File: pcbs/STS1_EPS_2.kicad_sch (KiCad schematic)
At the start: 11 parts, among them J1 DS1, J2 DS2, J5 RBF, J6 Antenna Deployment, J7 Inter-EPS, J8 UCI, U8 TPS259472ARPW

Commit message: Intermediate commit.
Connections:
- net UCI_COBC_NOT_RST: now reaches J8.10 (Pin_10)
- net UCI_COBC_SWDIO: now reaches J8.7 (Pin_7)
- net UCI_COBC_SWDCLK: now reaches J8.8 (Pin_8)
- net UCI_COBC_SWO: now reaches J8.9 (Pin_9)
- net UCI_COBC_3V3 renamed UCI_COBC_5V
- net UCI_COBC_UART_RX renamed UCI_COBC_UART_2
- net UCI_COBC_UART_TX renamed UCI_COBC_UART_1
- no-connect marks 7 -> 3
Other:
- sheet CSBI ports: added UCI_COBC_5V, UCI_COBC_NOT_RST, UCI_COBC_SWDCLK, UCI_COBC_SWDIO, UCI_COBC_SWO; removed none
- moved on the sheet: J8

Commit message: Signals to the bus gate should now be provided with supply voltage the proper way.
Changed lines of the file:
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@@
 	(wire
 		(pts
-			(xy 110.49 144.78) (xy 112.395 144.78)
+			(xy 108.585 153.67) (xy 110.49 153.67)
 		)
 		(stroke
@@
 	(wire
 		(pts
-			(xy 136.525 142.24) (xy 139.065 142.24)
+			(xy 134.62 151.13) (xy 137.16 151.13)
 		)
 		(stroke
@@
 	(wire
 		(pts
-			(xy 110.49 142.24) (xy 112.395 142.24)
+			(xy 108.585 151.13) (xy 110.49 151.13)
 		)
 		(stroke
@@
 	)
 	(label "BATT_RAW"
-		(at 110.49 144.78 180)
+		(at 108.585 153.67 180)
 		(fields_autoplaced yes)
 		(effects
@@
 	)
 	(label "MPPT_BUS"
-		(at 110.49 142.24 180)
+		(at 108.585 151.13 180)
 		(fields_autoplaced yes)
 		(effects
@@
 	)
 	(label "V_LOGIC"
-		(at 139.065 142.24 0)
+		(at 137.16 151.13 0)
 		(fields_autoplaced yes)
 		(effects
@@
 	)
 	(sheet
-		(at 112.395 140.335)
+		(at 110.49 149.225)
 		(size 24.13 6.35)
 		(fields_autoplaced yes)
@@
 		)
 		(property "Sheetname" "Logic Voltage"
-			(at 112.395 139.6234 0)
+			(at 110.49 148.5134 0)
 			(effects
 				(font
@@
 		)
 		(property "Sheetfile" "STS1_EPS_2_LOGIC_VOLTAGE.kicad_sch"
-			(at 112.395 147.2696 0)
+			(at 110.49 156.1596 0)
 			(effects
 				(font
@@
 		)
 		(pin "MPPT_BUS" input
-			(at 112.395 142.24 180)
+			(at 110.49 151.13 180)
 			(effects
 				(font
@@
 		)
 		(pin "BATT_RAW" input
-			(at 112.395 144.78 180)
+			(at 110.49 153.67 180)
 			(effects
 				(font
@@
 		)
 		(pin "V_LOGIC" output
-			(at 136.525 142.24 0)
+			(at 134.62 151.13 0)
 			(effects
 				(font

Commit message: Intermediate commit.
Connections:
- net GNDREF is gone; now on net GND: J8.2 (Pin_2)
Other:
- sheet Bus Gate ports: added V_LOGIC; removed none
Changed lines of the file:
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@@
 	(wire
 		(pts
-			(xy 44.45 180.34) (xy 43.815 180.34)
+			(xy 168.91 59.69) (xy 171.45 59.69)
 		)
 		(stroke
@@
 	(label "MPPT_BUS"
 		(at 108.585 151.13 180)
+		(fields_autoplaced yes)
+		(effects
+			(font
+				(size 1.27 1.27)
+			)
+			(justify right bottom)
+		)
+	)
+	(label "V_LOGIC"
+		(at 168.91 59.69 180)
 		(fields_autoplaced yes)
 		(effects
@@
 				(path "/38c03ff7-ea47-4d00-b37d-ddcaa7d87722"
 					(reference "#PWR03")
-					(unit 1)
-				)
-			)
-		)
-	)
-	(symbol
-		(lib_id "power:GNDREF")
-		(at 43.815 180.34 90)
-		(unit 1)
-		(exclude_from_sim no)
-		(in_bom yes)
-		(on_board yes)
-		(dnp no)
-		(fields_autoplaced yes)
-		(property "Reference" "#PWR0116"
-			(at 50.165 180.34 0)
-			(effects
-				(font
-					(size 1.27 1.27)
-				)
-				(hide yes)
-			)
-		)
-		(property "Value" "GNDREF"
-			(at 46.99 180.3399 90)
-			(effects
-				(font
-					(size 1.27 1.27)
-				)
-				(justify right)
-			)
-		)
-		(property "Footprint" ""
-			(at 43.815 180.34 0)
-			(effects
-				(font
-					(size 1.27 1.27)
-				)
-				(hide yes)
-			)
-		)
-		(property "Datasheet" ""
-			(at 43.815 180.34 0)
-			(effects
-				(font
-					(size 1.27 1.27)
-				)
-				(hide yes)
-			)
-		)
-		(property "Description" ""
-			(at 43.815 180.34 0)
-			(effects
-				(font
-					(size 1.27 1.27)
-				)
-				(hide yes)
-			)
-		)
-		(pin "1"
-		)
-		(instances
-			(project "STS1_EPS_2"
-				(path "/38c03ff7-ea47-4d00-b37d-ddcaa7d87722"
-					(reference "#PWR0116")
 					(unit 1)
 				)
@@
 				(path "/38c03ff7-ea47-4d00-b37d-ddcaa7d87722"
 					(reference "J5")
+					(unit 1)
+				)
+			)
+		)
+	)
+	(symbol
+		(lib_id "power:GND")
+		(at 44.45 180.34 90)
+		(unit 1)
+		(exclude_from_sim no)
+		(in_bom yes)
+		(on_board yes)
+		(dnp no)
+		(fields_autoplaced yes)
+		(property "Reference" "#PWR095"
+			(at 50.8 180.34 0)
+			(effects
+				(font
+					(size 1.27 1.27)
+				)
+				(hide yes)
+			)
+		)
+		(property "Value" "GND"
+			(at 47.625 180.3399 90)
+			(effects
+				(font
+					(size 1.27 1.27)
+				)
+				(justify right)
+			)
+		)
+		(property "Footprint" ""
+			(at 44.45 180.34 0)
+			(effects
+				(font
+					(size 1.27 1.27)
+				)
+				(hide yes)
+			)
+		)
+		(property "Datasheet" ""
+			(at 44.45 180.34 0)
+			(effects
+				(font
+					(size 1.27 1.27)
+				)
+				(hide yes)
+			)
+		)
+		(property "Description" ""
+			(at 44.45 180.34 0)
+			(effects
+				(font
+					(size 1.27 1.27)
+				)
+				(hide yes)
+			)
+		)
+		(pin "1"
+		)
+		(instances
+			(project "STS1_EPS_2"
+				(path "/38c03ff7-ea47-4d00-b37d-ddcaa7d87722"
+					(reference "#PWR095")
 					(unit 1)
 				)
@@
 			(effects
 				(font
+					(size 1.27 1.27)
+				)
+				(justify left)
+			)
+		)
+		(pin "V_LOGIC" input
+			(at 171.45 59.69 180)
+			(effects
+				(font

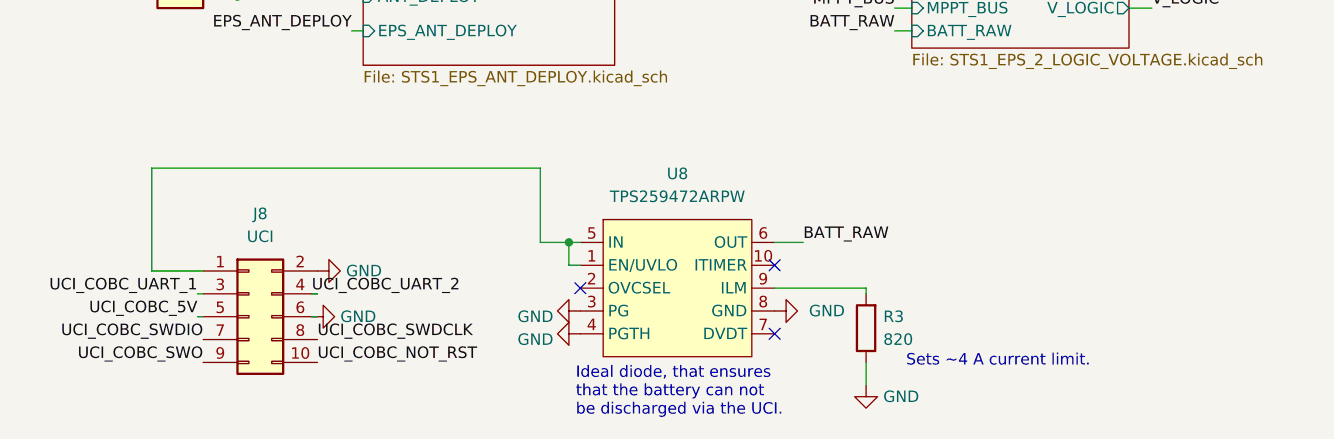
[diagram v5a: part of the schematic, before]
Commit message: Removed UCI connector from STS1_EPS_2 and merged UCI connector with J5 on STS1_EPS_1.
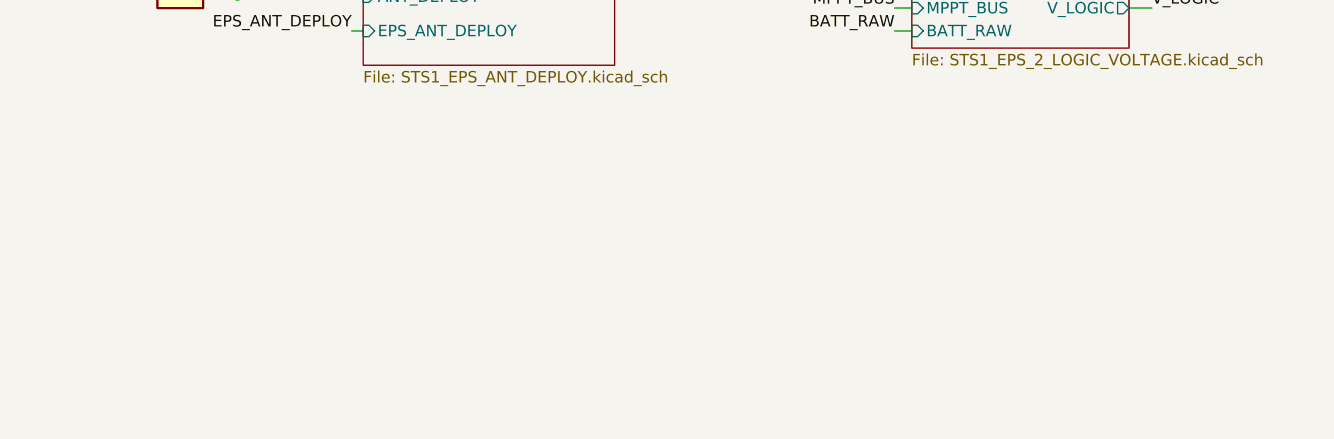
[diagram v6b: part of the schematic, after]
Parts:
- removed J8: UCI, STS_Connector:M80-85110YY, symbol Connector_Generic:Conn_02x05_Odd_Even
- removed R3: 820, Resistor_SMD:R_0805_2012Metric, symbol Device:R
- removed U8: TPS259472ARPW, STS_Package_DFN_QFN:TPS259472ARPWR, symbol STS_Power_Management:TPS259472ARPW
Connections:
- no-connect marks 3 -> 0
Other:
- note removed: "Ideal diode, that ensures that the battery can not be discharged via the UCI."
- note removed: "Sets ~4 A current limit."

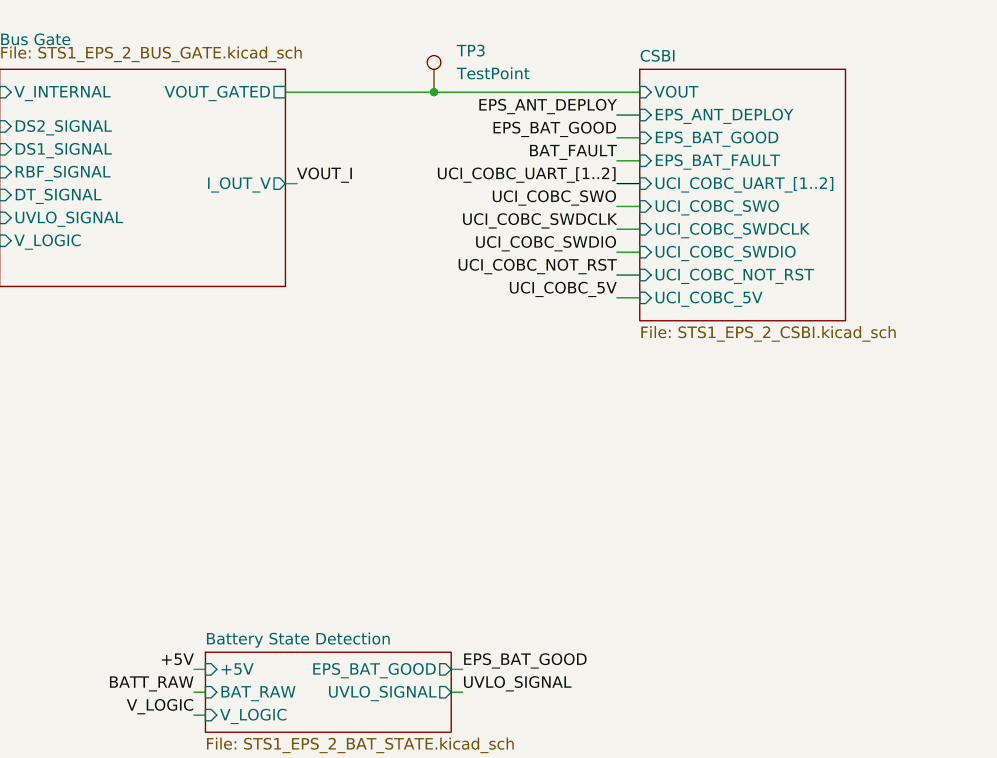
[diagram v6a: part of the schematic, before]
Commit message: Added even more ESD protection.
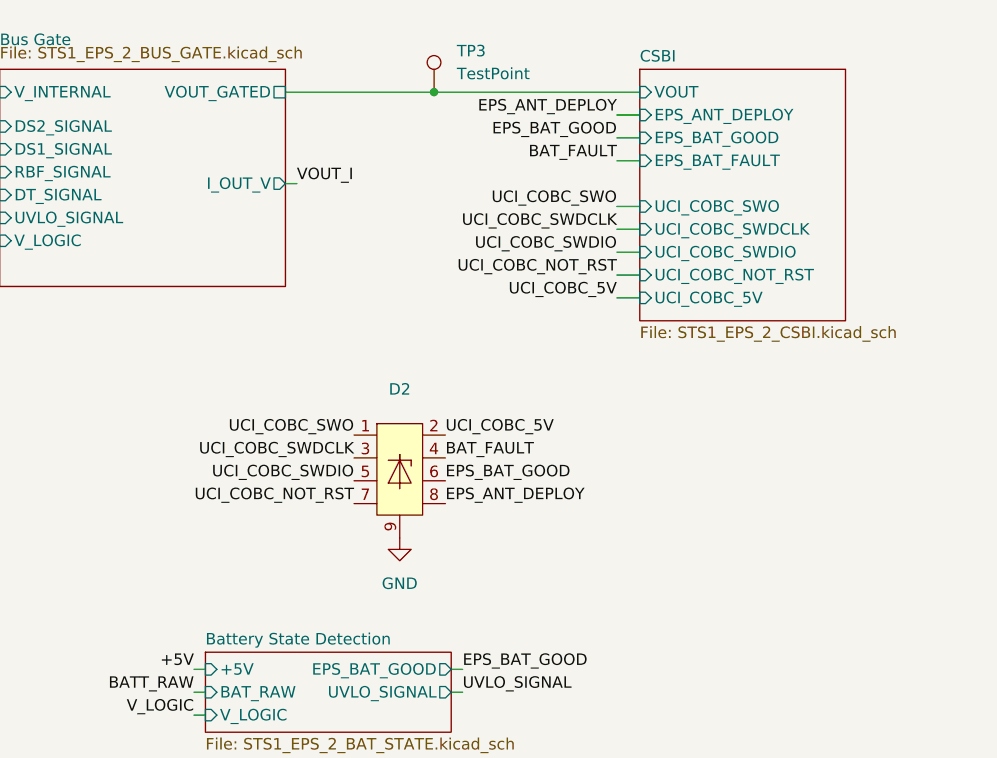
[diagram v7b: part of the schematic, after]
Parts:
- added D2: ~, STS_Misc:LLP1713-9L, symbol STS_Power_Management:VESD05A8A
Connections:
- net BAT_FAULT: now also D2.4
- net EPS_ANT_DEPLOY: now also D2.8
- net EPS_BAT_GOOD: now also D2.6
- net GND: now also D2.9
- net UCI_COBC_5V: now also D2.2
- net UCI_COBC_NOT_RST: now also D2.7
- net UCI_COBC_SWDCLK: now also D2.3
- net UCI_COBC_SWDIO: now also D2.5
- net UCI_COBC_SWO: now also D2.1
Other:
- sheet CSBI ports: added none; removed UCI_COBC_UART_[1..2]
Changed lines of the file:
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@@
-		)
-	)
-	(bus
-		(pts
-			(xy 240.03 53.34) (xy 242.57 53.34)
-		)
-		(stroke
-			(width 0)
-			(type default)
 		)
 	)
@@
 		)
 	)
+	(label "EPS_ANT_DEPLOY"
+		(at 220.98 88.9 0)
+		(fields_autoplaced yes)
+		(effects
+			(font
+				(size 1.27 1.27)
+			)
+			(justify left bottom)
+		)
+	)
+	(label "BAT_FAULT"
+		(at 220.98 83.82 0)
+		(fields_autoplaced yes)
+		(effects
+			(font
+				(size 1.27 1.27)
+			)
+			(justify left bottom)
+		)
+	)
 	(label "BAT_FAULT"
 		(at 190.5 141.605 180)
@@
 		)
 	)
-	(label "UCI_COBC_UART_[1..2]"
-		(at 240.03 53.34 180)
+	(label "UCI_COBC_SWDIO"
+		(at 210.82 86.36 180)
+		(fields_autoplaced yes)
+		(effects
+			(font
+				(size 1.27 1.27)
+			)
+			(justify right bottom)
+		)
+	)
+	(label "UCI_COBC_NOT_RST"
+		(at 210.82 88.9 180)
 		(fields_autoplaced yes)
 		(effects
@@
 		)
 	)
+	(label "UCI_COBC_5V"
+		(at 220.98 81.28 0)
+		(fields_autoplaced yes)
+		(effects
+			(font
+				(size 1.27 1.27)
+			)
+			(justify left bottom)
+		)
+	)
+	(label "EPS_BAT_GOOD"
+		(at 220.98 86.36 0)
+		(fields_autoplaced yes)
+		(effects
+			(font
+				(size 1.27 1.27)
+			)
+			(justify left bottom)
+		)
+	)
 	(label "V_LOGIC"
 		(at 109.855 92.71 180)
@@
 		)
 	)
+	(label "UCI_COBC_SWO"
+		(at 210.82 81.28 180)
+		(fields_autoplaced yes)
+		(effects
+			(font
+				(size 1.27 1.27)
+			)
+			(justify right bottom)
+		)
+	)
 	(label "EPS_BAT_GOOD"
 		(at 222.885 107.315 0)
@@
 			)
 			(justify left bottom)
+		)
+	)
+	(label "UCI_COBC_SWDCLK"
+		(at 210.82 83.82 180)
+		(fields_autoplaced yes)
+		(effects
+			(font
+				(size 1.27 1.27)
+			)
+			(justify right bottom)
 		)
 	)
@@
 	)
 	(symbol
+		(lib_id "STS_Power_Management:VESD05A8A")
+		(at 215.9 78.74 0)
+		(unit 1)
+		(exclude_from_sim no)
+		(in_bom yes)
+		(on_board yes)
+		(dnp no)
+		(fields_autoplaced yes)
+		(property "Reference" "D2"
+			(at 215.9 76.2 0)
+			(effects
+				(font
+					(size 1.27 1.27)
+				)
+			)
+		)
+		(property "Value" "~"
+			(at 215.9 78.74 0)
+			(effects
+				(font
+					(size 1.27 1.27)
+				)
+			)
+		)
+		(property "Footprint" "STS_Misc:LLP1713-9L"
+			(at 216.154 75.184 0)
+			(effects
+				(font
+					(size 1.27 1.27)
+				)
+				(hide yes)
+			)
+		)
+		(property "Datasheet" ""
+			(at 215.9 78.74 0)
+			(effects
+				(font
+					(size 1.27 1.27)
+				)
+				(hide yes)
+			)
+		)
+		(property "Description" ""
+			(at 215.9 78.74 0)
+			(effects
+				(font
+					(size 1.27 1.27)
+				)
+				(hide yes)
+			)
+		)
+		(pin "5"
+		)
+		(pin "7"
+		)
+		(pin "9"
+		)
+		(pin "8"
+		)
+		(pin "3"
+		)
+		(pin "6"
+		)
+		(pin "4"
+		)
+		(pin "1"
+		)
+		(pin "2"
+		)
+		(instances
+			(project "STS1_EPS_2"
+				(path "/38c03ff7-ea47-4d00-b37d-ddcaa7d87722"
+					(reference "D2")
+					(unit 1)
+				)
+			)
+		)
+	)
+	(symbol
 		(lib_id "power:GND")
 		(at 27.94 53.34 270)
@@
 				(path "/38c03ff7-ea47-4d00-b37d-ddcaa7d87722"
 					(reference "TP1")
+					(unit 1)
+				)
+			)
+		)
+	)
+	(symbol
+		(lib_id "power:GND")
+		(at 215.9 92.71 0)
+		(unit 1)
+		(exclude_from_sim no)
+		(in_bom yes)
+		(on_board yes)
+		(dnp no)
+		(fields_autoplaced yes)
+		(property "Reference" "#PWR025"
+			(at 215.9 99.06 0)
+			(effects
+				(font
+					(size 1.27 1.27)
+				)
+				(hide yes)
+			)
+		)
+		(property "Value" "GND"
+			(at 215.9 97.79 0)
+			(effects
+				(font
+					(size 1.27 1.27)
+				)
+			)
+		)
+		(property "Footprint" ""
+			(at 215.9 92.71 0)
+			(effects
+				(font
+					(size 1.27 1.27)
+				)
+				(hide yes)
+			)
+		)
+		(property "Datasheet" ""
+			(at 215.9 92.71 0)
+			(effects
+				(font
+					(size 1.27 1.27)
+				)
+				(hide yes)
+			)
+		)
+		(property "Description" ""
+			(at 215.9 92.71 0)
+			(effects
+				(font
+					(size 1.27 1.27)
+				)
+				(hide yes)
+			)
+		)
+		(pin "1"
+		)
+		(instances
+			(project "STS1_EPS_2"
+				(path "/38c03ff7-ea47-4d00-b37d-ddcaa7d87722"
+					(reference "#PWR025")
 					(unit 1)
 				)
@@
 			(effects
 				(font
-					(size 1.27 1.27)
-				)
-				(justify left)
-			)
-		)
-		(pin "UCI_COBC_UART_[1..2]" input
-			(at 242.57 53.34 180)
-			(effects
-				(font

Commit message: Fixed some warnings and errors.
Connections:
- net GND: now also J7.21 (Pin_21)
- net V_LOGIC: no longer J7.21 (Pin_21)
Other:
- note added: "5V is provided by STS1_EPS_1."
- note added: "V_LOGIC is a voltage that shall be available even when the CubeSat is in its undeployed state. It is needed to power the logic of the deployment switches, deployment timer and the bus gate."
- moved on the sheet: J1, J2, J5, TP2
